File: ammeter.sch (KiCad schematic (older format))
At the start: 29 parts, among them Q3 BC817, Q4 BC807, U12 LMC6482, U5 INA128

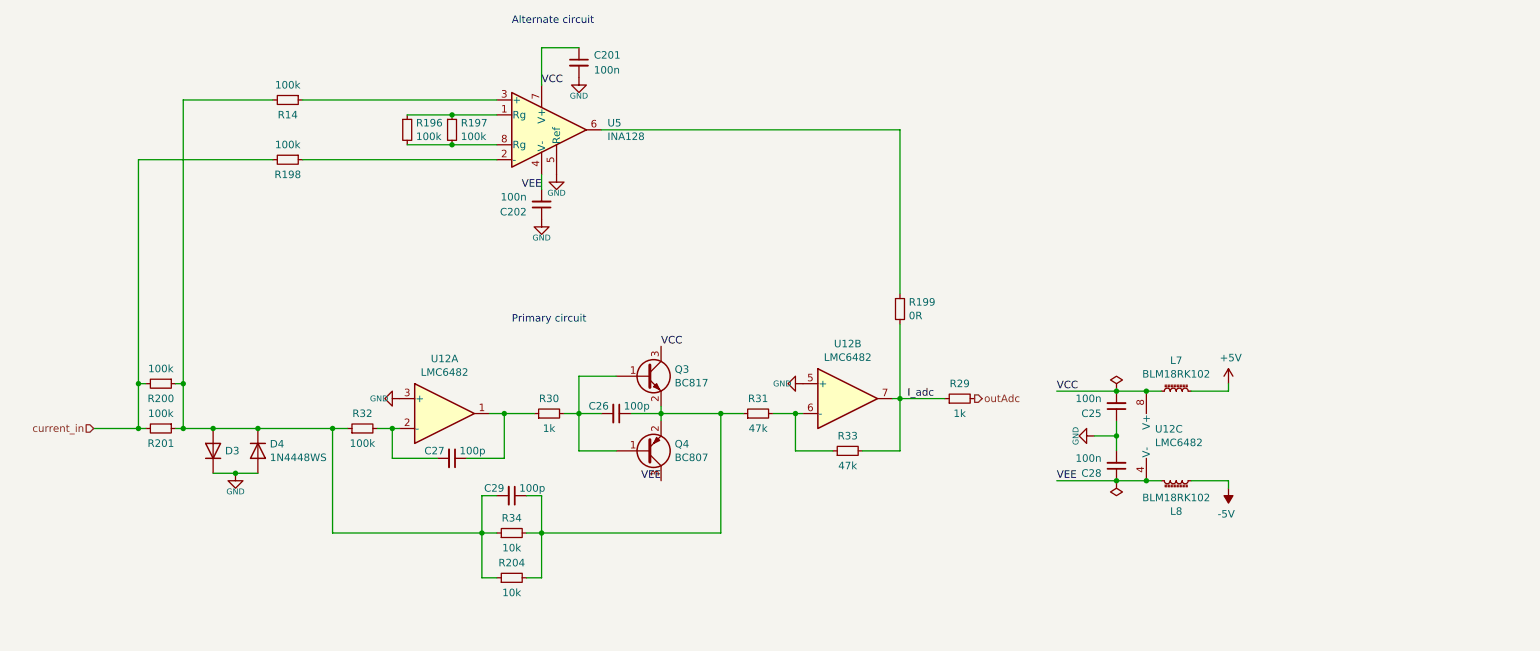
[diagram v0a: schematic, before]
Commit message: - PCB WiP - Pump output aligned
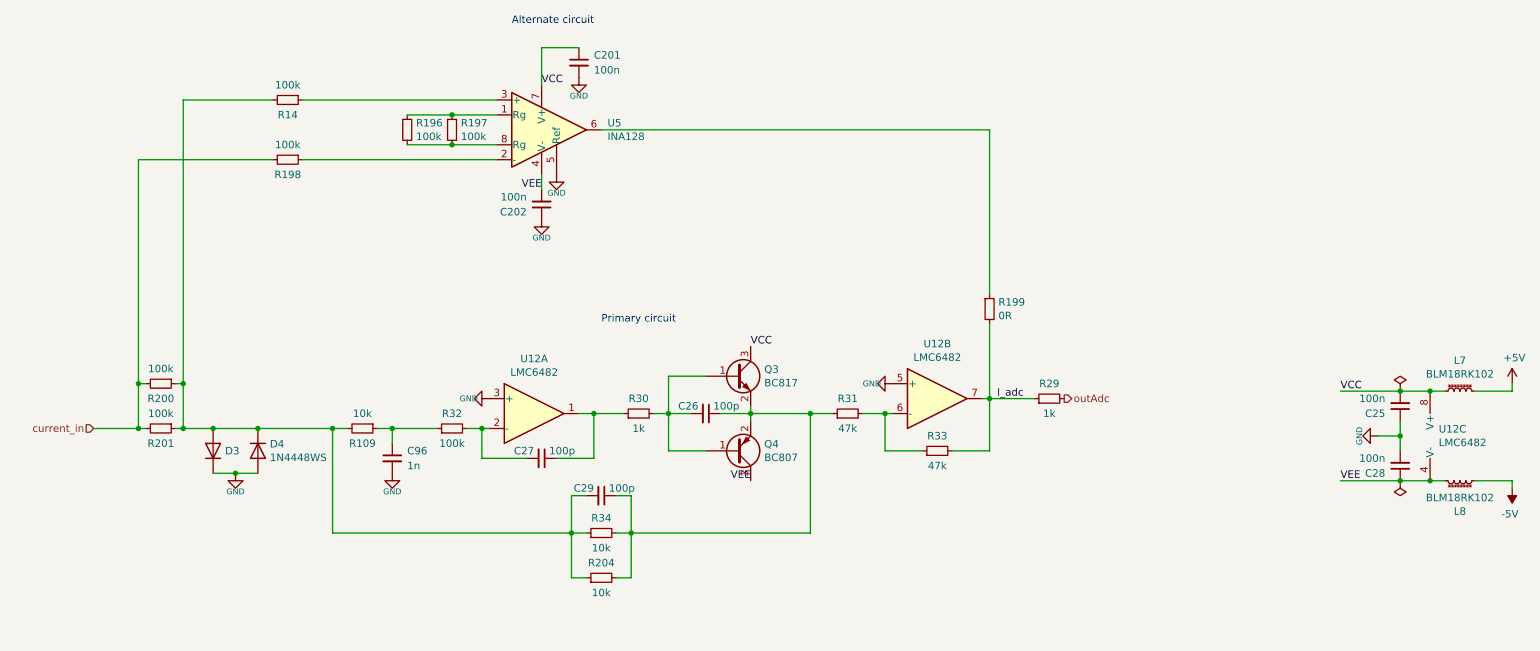
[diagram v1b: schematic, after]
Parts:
- added C96: 1n, Capacitor_SMD:C_0603_1608Metric, symbol Device:C_Small
- added R109: 10k, Resistor_SMD:R_0603_1608Metric_Pad1.05x0.95mm_HandSolder, symbol Device:R_Small
- R198, R199: footprint Resistor_SMD:R_0603_1608Metric_Pad1.05x0.95mm_HandSolder -> Resistor_SMD:R_0603_1608Metric
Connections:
- net GND: now also C96.2
- net at C29.2, D3.2 (A), D4.1 (K)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: now also R109.2; no longer R32.1
- new net: C96.1, R109.1, R32.1
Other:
- moved on the sheet: C25, C26, C27, C28, C29, L7, L8, Q3, Q4, R199, R204, R29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

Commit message: - PCB WiP
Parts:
- R109, R32: footprint Resistor_SMD:R_0603_1608Metric_Pad1.05x0.95mm_HandSolder -> Resistor_SMD:R_0603_1608Metric
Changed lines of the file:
@@
 F 0 "R32" V 3900 4000 50  0000 C CNN
 F 1 "100k" V 3700 4000 50  0000 C CNN
-F 2 "Resistor_SMD:R_0603_1608Metric_Pad1.05x0.95mm_HandSolder" V 3730 4000 50  0001 C CNN
+F 2 "Resistor_SMD:R_0603_1608Metric" V 3730 4000 50  0001 C CNN
 F 3 "~" H 3800 4000 50  0001 C CNN
 	1    3800 4000
@@
 F 0 "R109" V 3300 4000 50  0000 C CNN
 F 1 "10k" V 3100 4000 50  0000 C CNN
-F 2 "Resistor_SMD:R_0603_1608Metric_Pad1.05x0.95mm_HandSolder" V 3130 4000 50  0001 C CNN
+F 2 "Resistor_SMD:R_0603_1608Metric" V 3130 4000 50  0001 C CNN
 F 3 "~" H 3200 4000 50  0001 C CNN
 	1    3200 4000

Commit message: - PCB WiP
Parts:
- removed R201: 100k, Resistor_THT:R_Axial_DIN0207_L6.3mm_D2.5mm_P10.16mm_Horizontal, symbol Device:R_Small
- D3, D4: footprint miscellaneous_my:D_SOD-323-523-SMA_Universal_Handsoldering -> miscellaneous_my:D_SOD-323-523_HandSoldering
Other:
- moved on the sheet: R200
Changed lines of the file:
@@
 F 0 "D4" V 2454 4230 50  0000 L CNN
 F 1 "1N4448WS" V 2545 4230 50  0000 L CNN
-F 2 "miscellaneous_my:D_SOD-323-523-SMA_Universal_Handsoldering" H 2500 3975 50  0001 C CNN
+F 2 "miscellaneous_my:D_SOD-323-523_HandSoldering" H 2500 3975 50  0001 C CNN
 F 3 "https://www.vishay.com/docs/81387/1n4448ws.pdf" H 2500 4150 50  0001 C CNN
 	1    2500 4150
@@
 F 0 "D3" V 2200 4070 50  0000 R CNN
 F 1 "1N4448WS" V 2155 4070 50  0001 R CNN
-F 2 "miscellaneous_my:D_SOD-323-523-SMA_Universal_Handsoldering" H 2200 3975 50  0001 C CNN
+F 2 "miscellaneous_my:D_SOD-323-523_HandSoldering" H 2200 3975 50  0001 C CNN
 F 3 "https://www.vishay.com/docs/81387/1n4448ws.pdf" H 2200 4150 50  0001 C CNN
 	1    2200 4150
@@
 $Comp
 L Device:R_Small R?
-U 1 1 5FC6946F
+U 1 1 5FC6A856
 P 1850 4000
-AR Path="/5F40DCB9/5FC6946F" Ref="R?"  Part="1"
-AR Path="/5F479892/5FC6946F" Ref="R?"  Part="1"
-AR Path="/5FC6946F" Ref="R?"  Part="1"
-AR Path="/5F618AB9/5FC6946F" Ref="R201"  Part="1"
-F 0 "R201" V 1950 4000 50  0000 C CNN
+AR Path="/5F40DCB9/5FC6A856" Ref="R?"  Part="1"
+AR Path="/5F618AB9/5FC6A856" Ref="R200"  Part="1"
+F 0 "R200" V 1950 4000 50  0000 C CNN
 F 1 "100k" V 1750 4000 50  0000 C CNN
-F 2 "Resistor_THT:R_Axial_DIN0207_L6.3mm_D2.5mm_P10.16mm_Horizontal" V 1780 4000 50  0001 C CNN
+F 2 "Resistor_SMD:R_0603_1608Metric_Pad1.05x0.95mm_HandSolder" V 1780 4000 50  0001 C CNN
 F 3 "~" H 1850 4000 50  0001 C CNN
 	1    1850 4000
 	0    1    1    0
 $EndComp
-$Comp
-L Device:R_Small R?
-U 1 1 5FC6A856
-P 1850 3700
-AR Path="/5F40DCB9/5FC6A856" Ref="R?"  Part="1"
-AR Path="/5F618AB9/5FC6A856" Ref="R200"  Part="1"
-F 0 "R200" V 1950 3700 50  0000 C CNN
-F 1 "100k" V 1750 3700 50  0000 C CNN
-F 2 "Resistor_SMD:R_0603_1608Metric_Pad1.05x0.95mm_HandSolder" V 1780 3700 50  0001 C CNN
-F 3 "~" H 1850 3700 50  0001 C CNN
-	1    1850 3700
-	0    1    1    0
-$EndComp
-Wire Wire Line
-	2000 4000 2000 3700
-Wire Wire Line
-	2000 3700 1950 3700
 Wire Wire Line
 	2000 4000 1950 4000
@@
 Wire Wire Line
 	1750 4000 1700 4000
-Wire Wire Line
-	1700 4000 1700 3700
-Wire Wire Line
-	1700 3700 1750 3700
 Wire Wire Line
 	1700 4000 1400 4000
@@
 	4100 1800 2800 1800
 Wire Wire Line
-	2000 1800 2000 3700
-Connection ~ 2000 3700
-Wire Wire Line
 	4100 2200 2800 2200
-Wire Wire Line
-	1700 2200 1700 3700
-Connection ~ 1700 3700
 $Comp
 L Device:R_Small R?
@@
 Wire Wire Line
 	3400 4000 3700 4000
+Wire Wire Line
+	1700 2200 1700 4000
+Wire Wire Line
+	2000 1800 2000 4000
 $EndSCHEMATC

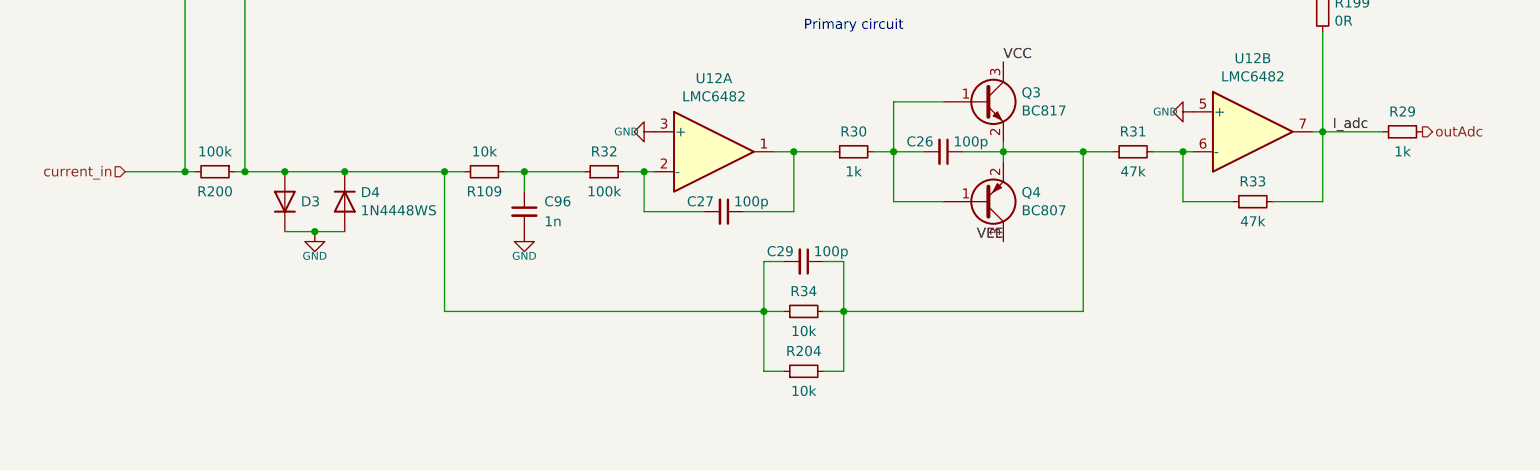
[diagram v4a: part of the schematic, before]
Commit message: - as-built changes - add custom library elements
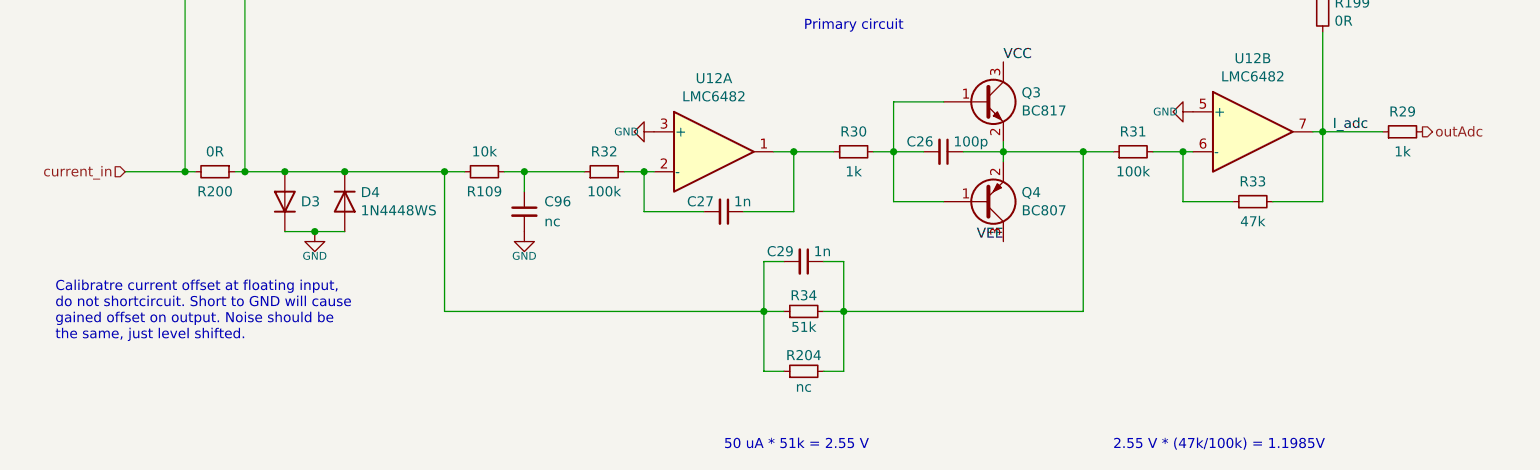
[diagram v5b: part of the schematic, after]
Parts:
- C27, C29: value 100p -> 1n
- C96: value 1n -> nc
- R200: value 100k -> 0R
- R204: value 10k -> nc
- R31: value 47k -> 100k
- R34: value 10k -> 51k
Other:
- note added: "2.55 V * (47k/100k) = 1.1985V"
- note added: "50 uA * 51k = 2.55 V"
- note added: "Calibratre current offset at floating input, \ndo not shortcircuit. Short to GND will cause \ngained offset on output. Noise should be \nthe same, just level shifted."
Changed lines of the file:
@@
 $Descr A4 11693 8268
 encoding utf-8
-Sheet 4 10
-Title ""
-Date ""
-Rev ""
-Comp ""
+Sheet 3 10
+Title "Amperomierz"
+Date "2021-01-18"
+Rev "1.0"
+Comp "Łukasz Sitarek"
 Comment1 ""
 Comment2 ""
@@
 AR Path="/5F40DCB9/5F618EB7" Ref="R?"  Part="1"
 AR Path="/5F618AB9/5F618EB7" Ref="R34"  Part="1"
-F 0 "R34" V 4900 4700 50  0000 C CNN
-F 1 "10k" V 4700 4700 50  0000 C CNN
+F 0 "R34" V 4850 4700 50  0000 C TNN
+F 1 "51k" V 4750 4700 50  0000 C BNN
 F 2 "Resistor_SMD:R_0603_1608Metric_Pad1.05x0.95mm_HandSolder" V 4730 4700 50  0001 C CNN
 F 3 "~" H 4800 4700 50  0001 C CNN
@@
 AR Path="/5F618AB9/5F618EFF" Ref="C29"  Part="1"
 F 0 "C29" V 4750 4400 50  0000 R CNN
-F 1 "100p" V 4750 4500 50  0000 L CNN
+F 1 "1n" V 4750 4500 50  0000 L CNN
 F 2 "Capacitor_SMD:C_0603_1608Metric_Pad1.05x0.95mm_HandSolder" H 4800 4450 50  0001 C CNN
 F 3 "~" H 4800 4450 50  0001 C CNN
@@
 AR Path="/5F618AB9/5F618F0F" Ref="R31"  Part="1"
 F 0 "R31" V 6550 3900 50  0000 C CNN
-F 1 "47k" V 6350 3900 50  0000 C CNN
+F 1 "100k" V 6350 3900 50  0000 C CNN
 F 2 "Resistor_SMD:R_0603_1608Metric" V 6380 3900 50  0001 C CNN
 F 3 "~" H 6450 3900 50  0001 C CNN
@@
 AR Path="/5F618AB9/5FC12659" Ref="C27"  Part="1"
 F 0 "C27" V 4350 4150 50  0000 R CNN
-F 1 "100p" V 4350 4250 50  0000 L CNN
+F 1 "1n" V 4350 4250 50  0000 L CNN
 F 2 "Capacitor_SMD:C_0603_1608Metric" H 4400 4200 50  0001 C CNN
 F 3 "~" H 4400 4200 50  0001 C CNN
@@
 AR Path="/5F618AB9/5FC6A856" Ref="R200"  Part="1"
 F 0 "R200" V 1950 4000 50  0000 C CNN
-F 1 "100k" V 1750 4000 50  0000 C CNN
+F 1 "0R" V 1750 4000 50  0000 C CNN
 F 2 "Resistor_SMD:R_0603_1608Metric_Pad1.05x0.95mm_HandSolder" V 1780 4000 50  0001 C CNN
 F 3 "~" H 1850 4000 50  0001 C CNN
@@
 AR Path="/5F40DCB9/5FA9EA22" Ref="R?"  Part="1"
 AR Path="/5F618AB9/5FA9EA22" Ref="R204"  Part="1"
-F 0 "R204" V 4900 5000 50  0000 C CNN
-F 1 "10k" V 4700 5000 50  0000 C CNN
+F 0 "R204" V 4850 5000 50  0000 C TNN
+F 1 "nc" V 4750 5000 50  0000 C BNN
 F 2 "Resistor_SMD:R_1206_3216Metric" V 4730 5000 50  0001 C CNN
 F 3 "~" H 4800 5000 50  0001 C CNN
@@
 AR Path="/5F618AB9/5FAE5C96" Ref="C96"  Part="1"
 F 0 "C96" H 3500 4250 50  0000 L CNN
-F 1 "1n" H 3500 4150 50  0000 L CNN
+F 1 "nc" H 3500 4150 50  0000 L CNN
 F 2 "Capacitor_SMD:C_0603_1608Metric" H 3400 4200 50  0001 C CNN
 F 3 "~" H 3400 4200 50  0001 C CNN
@@
 Wire Wire Line
 	2000 1800 2000 4000
+Text Notes 4400 5400 0    50   ~ 0
+50 uA * 51k = 2.55 V
+Text Notes 6350 5400 0    50   ~ 0
+2.55 V * (47k/100k) = 1.1985V
+Text Notes 1050 4850 0    50   ~ 0
+Calibratre current offset at floating input, \ndo not shortcircuit. Short to GND will cause \ngained offset on output. Noise should be \nthe same, just level shifted.
 $EndSCHEMATC
